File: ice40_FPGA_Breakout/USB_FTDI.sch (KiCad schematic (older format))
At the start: 0 parts

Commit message: USB to FTDI partial schematic
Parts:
- added C? (x18): C, symbol C
- added D?: NUP2105L, TO_SOT_Packages_SMD:SOT-23, symbol NUP2105L
- added D?: D_Schottky, symbol D_Schottky
- added J?: USB_B_Micro, symbol USB_B_Micro
- added L? (x5): Ferrite_Bead, symbol Ferrite_Bead
- added R? (x8): R, symbol R
- added U?: FT2232H, symbol FT2232H
- added U?: 93LCxxC, symbol 93LCxxC
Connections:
- net labels added: GND
- wire segments 0 -> 116
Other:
- note added: "4.7V from USB"

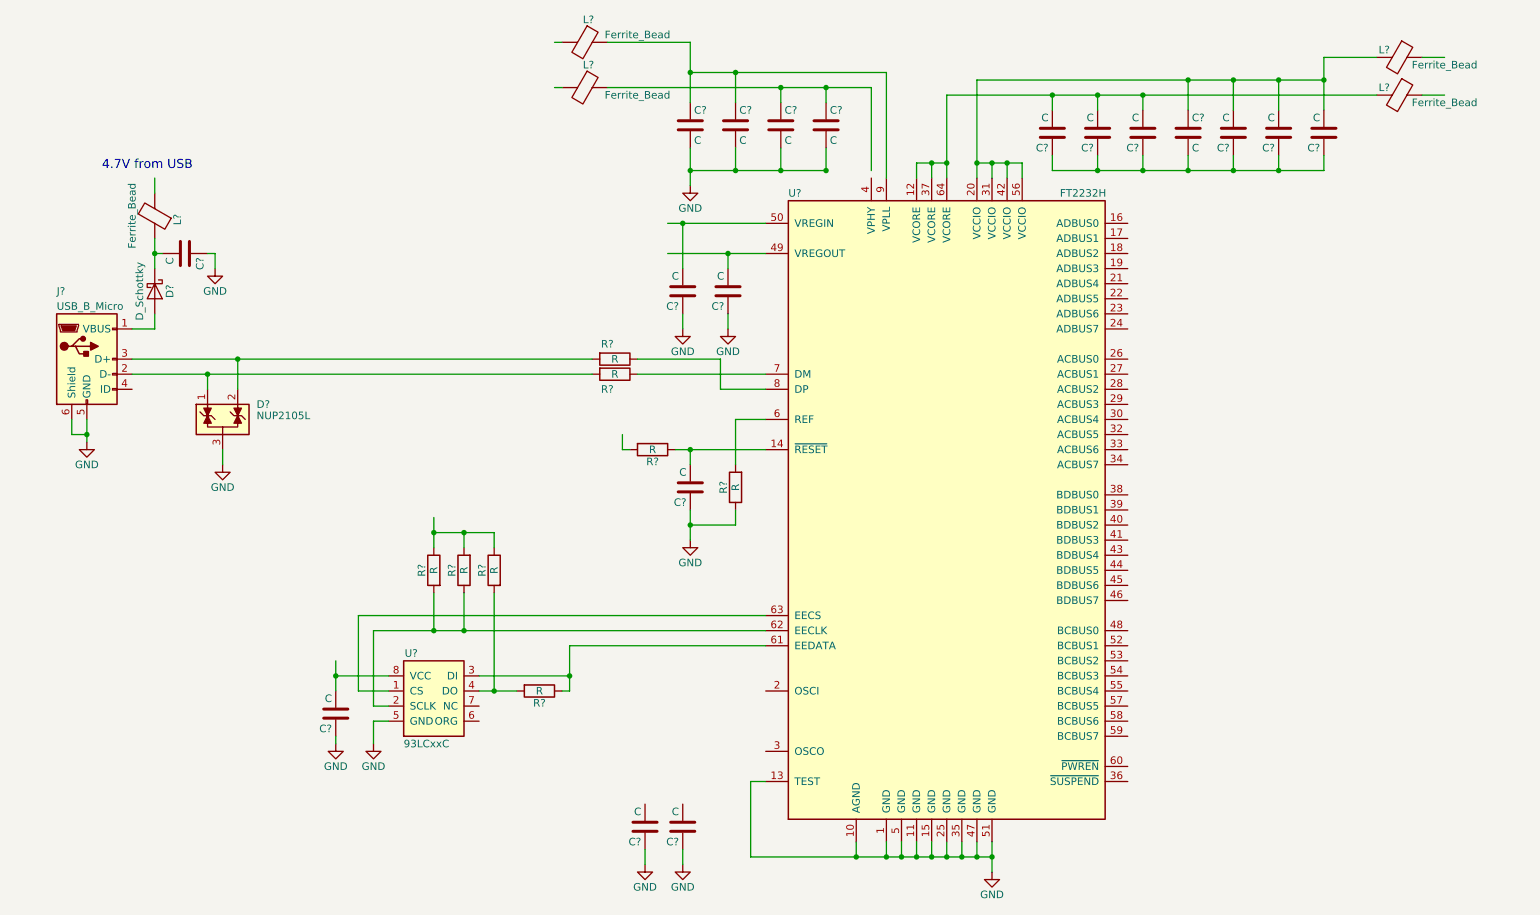
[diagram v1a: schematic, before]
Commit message: FTDI, iCE40 chip differential pair schematic
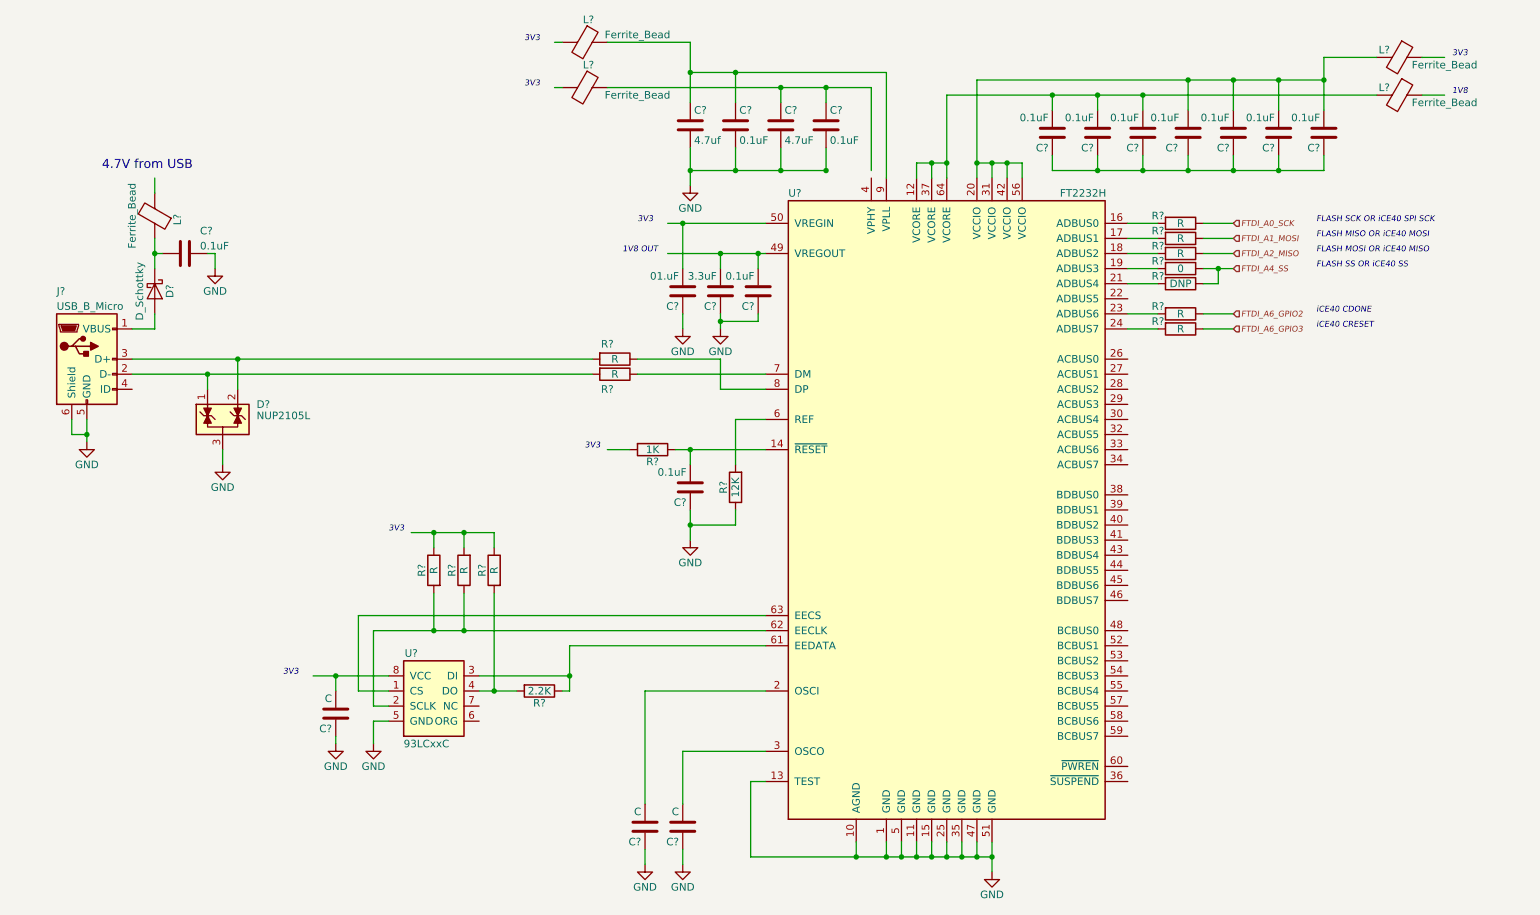
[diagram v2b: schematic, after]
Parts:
- added C?: 0.1uF, symbol C
- added R? (x5): R, symbol R
- added R?: 0, symbol R
- added R?: DNP, symbol R
- C? (x11): value C -> 0.1uF
- C?: value C -> 4.7uf
- C?: value C -> 4.7uF
- C?: value C -> 01.uF
- C?: value C -> 3.3uF
- R?: value R -> 2.2K
- R?: value R -> 12K
- R?: value R -> 1K
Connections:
- net labels added: FTDI_A0_SCK, FTDI_A1_MOSI, FTDI_A2_MISO, FTDI_A4_SS, FTDI_A6_GPIO2, FTDI_A6_GPIO3
- wire segments 116 -> 137
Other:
- note added: "1V8"
- note added: "1V8 OUT"
- note added: "3V3"
- note added: "FLASH MISO OR iCE40 MOSI"
- note added: "FLASH MOSI OR iCE40 MISO"
- note added: "FLASH SCK OR iCE40 SPI SCK"
- note added: "FLASH SS OR iCE40 SS"
- note added: "iCE40 CDONE"
- note added: "iCE40 CRESET"
- moved on the sheet: C?

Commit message: Added SO-DIMM header, ice40 IO and FTDI power
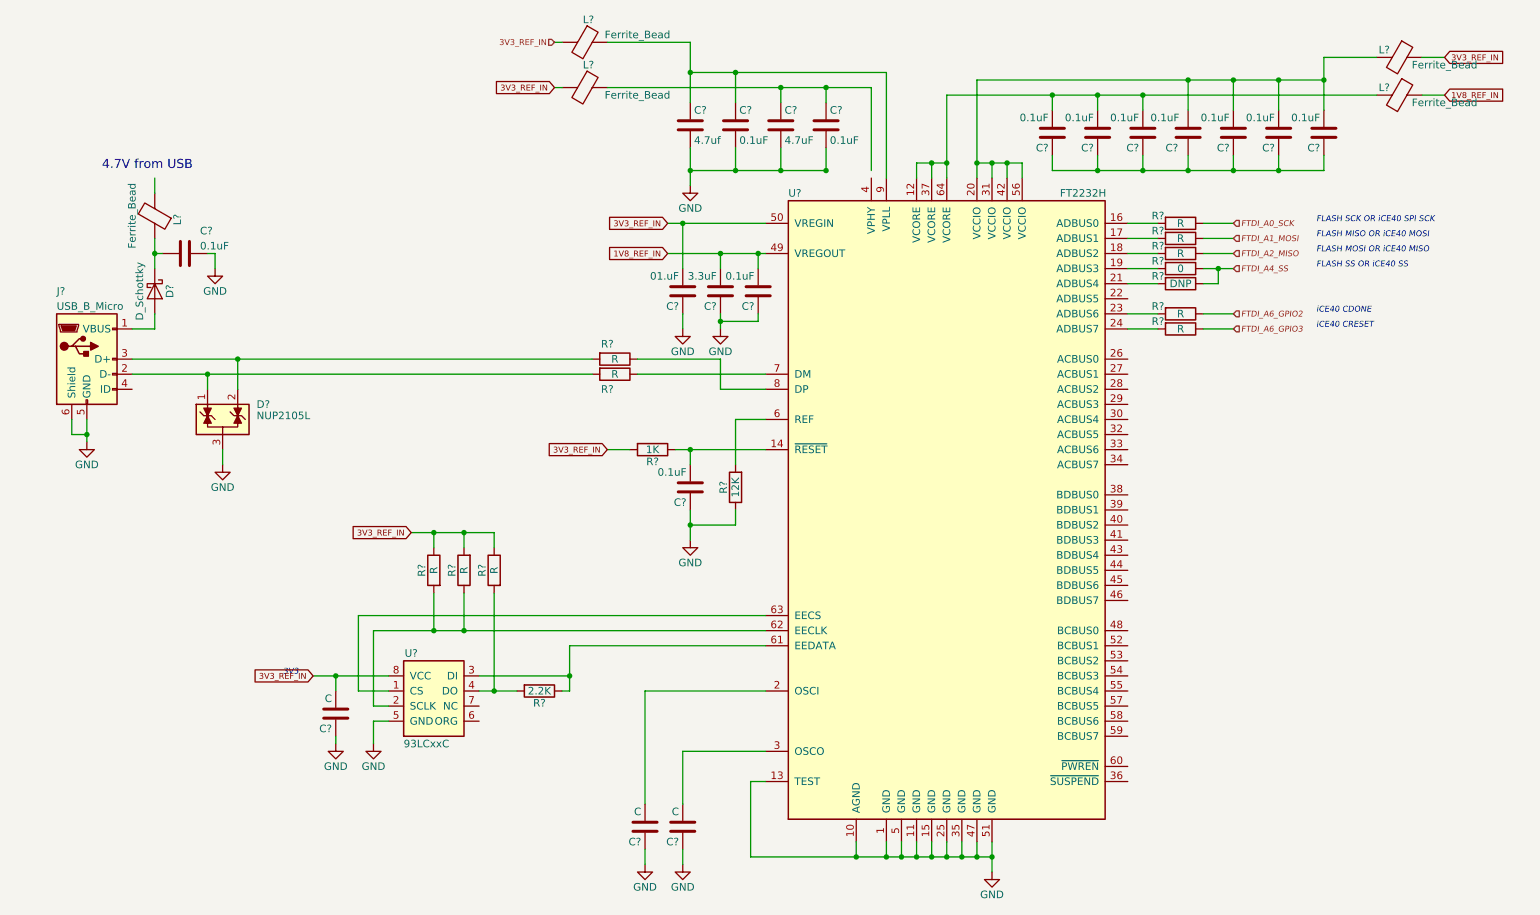
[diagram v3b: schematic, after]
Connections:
- net labels added: 1V8_REF_IN, 3V3_REF_IN
- wire segments 137 -> 188
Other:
- note removed: "1V8"
- note removed: "1V8 OUT"
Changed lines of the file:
@@
 $EndComp
 Wire Wire Line
-	7550 5950 7550 6150
-Wire Wire Line
-	5950 6050 7550 6050
+	7550 5950 7550 6050
+Wire Wire Line
+	7550 6050 7550 6150
+Wire Wire Line
+	5950 6050 6650 6050
+Wire Wire Line
+	6650 6050 6850 6050
+Wire Wire Line
+	6850 6050 6950 6050
+Wire Wire Line
+	6950 6050 7050 6050
+Wire Wire Line
+	7050 6050 7150 6050
+Wire Wire Line
+	7150 6050 7250 6050
+Wire Wire Line
+	7250 6050 7350 6050
+Wire Wire Line
+	7350 6050 7450 6050
+Wire Wire Line
+	7450 6050 7550 6050
 Wire Wire Line
 	6650 5950 6650 6050
@@
 Connection ~ 2350 2850
 Wire Wire Line
-	1550 3150 1550 3300
+	1550 3150 1550 3250
+Wire Wire Line
+	1550 3250 1550 3300
 Wire Wire Line
 	1450 3150 1450 3250
@@
 	5200 2750 5750 2750
 Wire Wire Line
-	1850 2850 4900 2850
-Wire Wire Line
-	1850 2750 4900 2750
-Wire Wire Line
-	5450 3350 6050 3350
+	1850 2850 2350 2850
+Wire Wire Line
+	2350 2850 4900 2850
+Wire Wire Line
+	1850 2750 2550 2750
+Wire Wire Line
+	2550 2750 4900 2750
+Wire Wire Line
+	5450 3350 5550 3350
+Wire Wire Line
+	5550 3350 6050 3350
 Wire Wire Line
 	5550 3450 5550 3350
 Connection ~ 5550 3350
 Wire Wire Line
-	5550 3750 5550 3950
+	5550 3750 5550 3850
+Wire Wire Line
+	5550 3850 5550 3950
 Connection ~ 5550 3850
 Wire Wire Line
@@
 Connection ~ 2000 2050
 Wire Wire Line
-	2000 1950 2000 2150
+	2000 1950 2000 2050
+Wire Wire Line
+	2000 2050 2000 2150
 Wire Wire Line
 	2000 1650 2000 1550
@@
 	3350 4450 6050 4450
 Wire Wire Line
-	3450 4550 6050 4550
-Wire Wire Line
-	4150 4950 4400 4950
-Wire Wire Line
-	3050 4850 3550 4850
+	3450 4550 3850 4550
+Wire Wire Line
+	3850 4550 4050 4550
+Wire Wire Line
+	4050 4550 6050 4550
+Wire Wire Line
+	4150 4950 4250 4950
+Wire Wire Line
+	4250 4950 4400 4950
+Wire Wire Line
+	3050 4850 3200 4850
+Wire Wire Line
+	3200 4850 3550 4850
 Wire Wire Line
 	3200 4850 3200 4950
 Wire Wire Line
-	4750 4650 4750 4950
+	4750 4650 4750 4850
+Wire Wire Line
+	4750 4850 4750 4950
 Wire Wire Line
 	4750 4950 4700 4950
@@
 Connection ~ 4050 4550
 Wire Wire Line
-	3700 3900 4250 3900
+	3700 3900 3850 3900
+Wire Wire Line
+	3850 3900 4050 3900
+Wire Wire Line
+	4050 3900 4250 3900
 Wire Wire Line
 	3850 3900 3850 4000
@@
 	5500 6000 5500 6100
 Wire Wire Line
-	5550 1350 5550 1600
+	5550 1350 5550 1500
+Wire Wire Line
+	5550 1500 5550 1600
 Wire Wire Line
 	6450 1500 6450 1350
@@
 	7050 1550 7050 1450
 Wire Wire Line
-	7050 1450 7250 1450
-Wire Wire Line
-	7250 1000 7250 1550
+	7050 1450 7150 1450
+Wire Wire Line
+	7150 1450 7250 1450
+Wire Wire Line
+	7250 1000 7250 1450
+Wire Wire Line
+	7250 1450 7250 1550
 Wire Wire Line
 	7150 1550 7150 1450
 Connection ~ 7150 1450
 Wire Wire Line
-	7450 900  7450 1550
-Wire Wire Line
-	7450 1450 7750 1450
+	7450 900  7450 1450
+Wire Wire Line
+	7450 1450 7450 1550
+Wire Wire Line
+	7450 1450 7550 1450
+Wire Wire Line
+	7550 1450 7650 1450
+Wire Wire Line
+	7650 1450 7750 1450
 Wire Wire Line
 	7750 1450 7750 1550
@@
 Connection ~ 7450 1450
 Wire Wire Line
-	5550 1500 6450 1500
+	5550 1500 5850 1500
+Wire Wire Line
+	5850 1500 6150 1500
+Wire Wire Line
+	6150 1500 6450 1500
 Connection ~ 5550 1500
 Wire Wire Line
@@
 	6150 1050 6150 950
 Wire Wire Line
-	5000 950  6750 950
+	5000 950  6150 950
+Wire Wire Line
+	6150 950  6450 950
+Wire Wire Line
+	6450 950  6750 950
 Wire Wire Line
 	6450 950  6450 1050
 Connection ~ 6450 950
 Wire Wire Line
-	5550 650  5550 1050
-Wire Wire Line
-	5550 850  6850 850
+	5550 650  5550 850
+Wire Wire Line
+	5550 850  5550 1050
+Wire Wire Line
+	5550 850  5850 850
+Wire Wire Line
+	5850 850  6850 850
 Wire Wire Line
 	5850 850  5850 1050
@@
 	7950 1100 7950 1000
 Wire Wire Line
-	7250 1000 10100 1000
+	7250 1000 7950 1000
+Wire Wire Line
+	7950 1000 8250 1000
+Wire Wire Line
+	8250 1000 8550 1000
+Wire Wire Line
+	8550 1000 10100 1000
 Wire Wire Line
 	8550 1000 8550 1100
@@
 	8850 1100 8850 900
 Wire Wire Line
-	7450 900  9750 900
-Wire Wire Line
-	9750 750  9750 1100
+	7450 900  8850 900
+Wire Wire Line
+	8850 900  9150 900
+Wire Wire Line
+	9150 900  9450 900
+Wire Wire Line
+	9450 900  9750 900
+Wire Wire Line
+	9750 750  9750 900
+Wire Wire Line
+	9750 900  9750 1100
 Wire Wire Line
 	9450 1100 9450 900
@@
 	7950 1400 7950 1500
 Wire Wire Line
-	7950 1500 9750 1500
+	7950 1500 8250 1500
+Wire Wire Line
+	8250 1500 8550 1500
+Wire Wire Line
+	8550 1500 8850 1500
+Wire Wire Line
+	8850 1500 9150 1500
+Wire Wire Line
+	9150 1500 9450 1500
+Wire Wire Line
+	9450 1500 9750 1500
 Wire Wire Line
 	8550 1500 8550 1400
@@
 	5250 6000 5250 6100
 Wire Wire Line
-	5400 2050 6050 2050
+	5400 2050 5750 2050
+Wire Wire Line
+	5750 2050 6000 2050
+Wire Wire Line
+	6000 2050 6050 2050
 Wire Wire Line
 	5750 2050 5750 2150
 Wire Wire Line
-	5400 1850 6050 1850
+	5400 1850 5500 1850
+Wire Wire Line
+	5500 1850 6050 1850
 Wire Wire Line
 	5500 1850 5500 2150
@@
 	5500 2550 5500 2450
 Wire Wire Line
-	5750 2450 5750 2550
+	5750 2450 5750 2500
+Wire Wire Line
+	5750 2500 5750 2550
 Connection ~ 5750 2050
 Connection ~ 5500 1850
@@
 Wire Wire Line
 	5250 4950 5250 5700
-Text Notes 4450 650  0    39   Italic 0
-3V3
-Text Notes 4450 950  0    39   Italic 0
-3V3
-Text Notes 10600 750  0    39   Italic 0
-3V3
-Text Notes 10600 1000 0    39   Italic 0
-1V8
-Text Notes 4850 3350 0    39   Italic 0
-3V3
-Text Notes 3550 3900 0    39   Italic 0
-3V3
 Text Notes 2850 4850 0    39   Italic 0
 3V3
@@
 	8950 2050 9150 2050
 Wire Wire Line
-	8950 2150 9150 2150
+	8950 2150 9050 2150
+Wire Wire Line
+	9050 2150 9150 2150
 Wire Wire Line
 	8950 2450 9150 2450
@@
 Text HLabel 9150 2150 2    39   Input Italic 0
 FTDI_A4_SS
-Text Notes 5200 1850 0    39   Italic 0
-3V3
-Text Notes 5100 2050 0    39   Italic 0
-1V8 OUT
 $Comp
 L C C?
@@
 Text Notes 9700 2550 0    39   Italic 0
 iCE40 CRESET
+Text HLabel 4650 650  0    39   Input ~ 0
+3V3_REF_IN
+Text GLabel 4650 950  0    39   Input ~ 0
+3V3_REF_IN
+Text GLabel 5400 1850 0    39   Input ~ 0
+3V3_REF_IN
+Text GLabel 5400 2050 0    39   Input ~ 0
+1V8_REF_IN
+Text GLabel 5000 3350 0    39   Input ~ 0
+3V3_REF_IN
+Text GLabel 3700 3900 0    39   Input ~ 0
+3V3_REF_IN
+Text GLabel 3050 4850 0    39   Input ~ 0
+3V3_REF_IN
+Text GLabel 10550 750  2    39   Input ~ 0
+3V3_REF_IN
+Text GLabel 10550 1000 2    39   Input ~ 0
+1V8_REF_IN
 $EndSCHEMATC

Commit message: R/C value updated to FTDI section and also BD port UART logic added
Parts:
- added D? (x2): LED, symbol LED
- added R? (x2): 330, symbol R
- R? (x3): value R -> 10K
- R? (x7): value R -> 0
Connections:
- net 3V3_REF_IN: now also R?.1, R?.1
- net FTDI_TXD: now reaches U?.38 (BDBUS0)
- net FTDI_RXD: now reaches U?.39 (BDBUS1)
- net ~FTDI_RTS: now reaches U?.40 (BDBUS2)
- net ~FTDI_CTS: now reaches U?.41 (BDBUS3)
- net FTDI_TXDEN: now reaches U?.48 (BCBUS0)
- net at U?.54 (BCBUS3): now also D?.1 (K)
- net at U?.55 (BCBUS4): now also D?.1 (K)
- new net: D?.2 (A), R?.2 (x2)
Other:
- note removed: "3V3"
